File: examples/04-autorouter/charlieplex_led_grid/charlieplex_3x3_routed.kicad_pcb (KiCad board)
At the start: 2 copper layers, 50 x 55 mm, 14 parts, among them U1 MCU

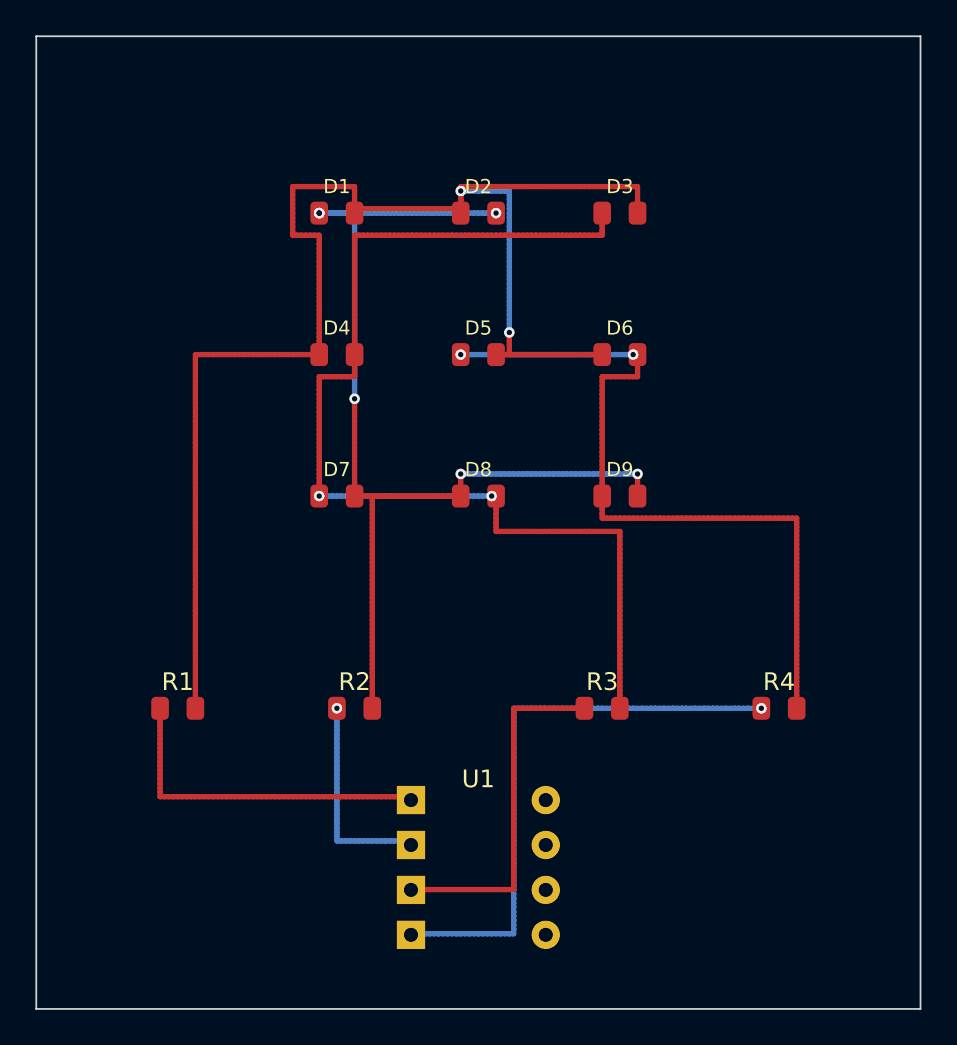
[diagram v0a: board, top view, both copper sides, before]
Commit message: fix(sexp): kicad-cli compatibility and add voltage divider example
- Change default stroke type from "solid" to "default"
- Simplify junction_node to omit rotation angle and color field
- Update schematic version to 20231120 for compatibility
- Add *.rpt to gitignore
- Add voltage divider test example with manufacturing outputs
- Update charlieplex example with latest routing

🤖 Generated with [Claude Code](https://claude.com/claude-code)

Co-Authored-By: Claude Opus 4.5 <noreply@anthropic.com>
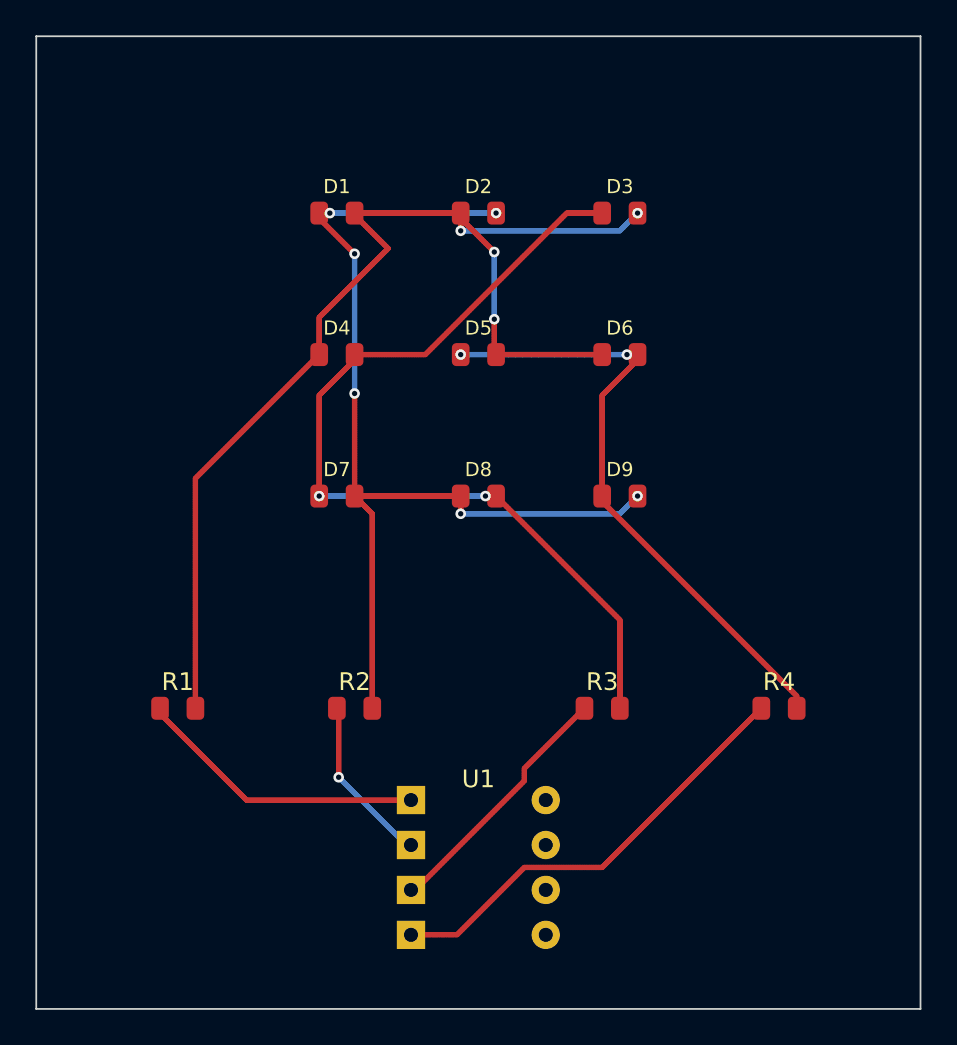
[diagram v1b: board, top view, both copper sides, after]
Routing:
- net NODE_A: track 82.5 -> 65.5 mm, vias 2 -> 4
- net NODE_C: track 61.0 -> 51.0 mm
- net LINE_D: track 32.9 -> 25.1 mm, vias 1 -> 0
- net NODE_D: track 43.0 -> 35.4 mm
- net LINE_C: track 20.4 -> 14.5 mm
- net NODE_B: track 59.5 -> 56.7 mm
- net LINE_A: track 19.3 -> 16.5 mm
- net LINE_B: track 11.8 -> 9.65 mm
